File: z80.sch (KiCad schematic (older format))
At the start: 0 parts

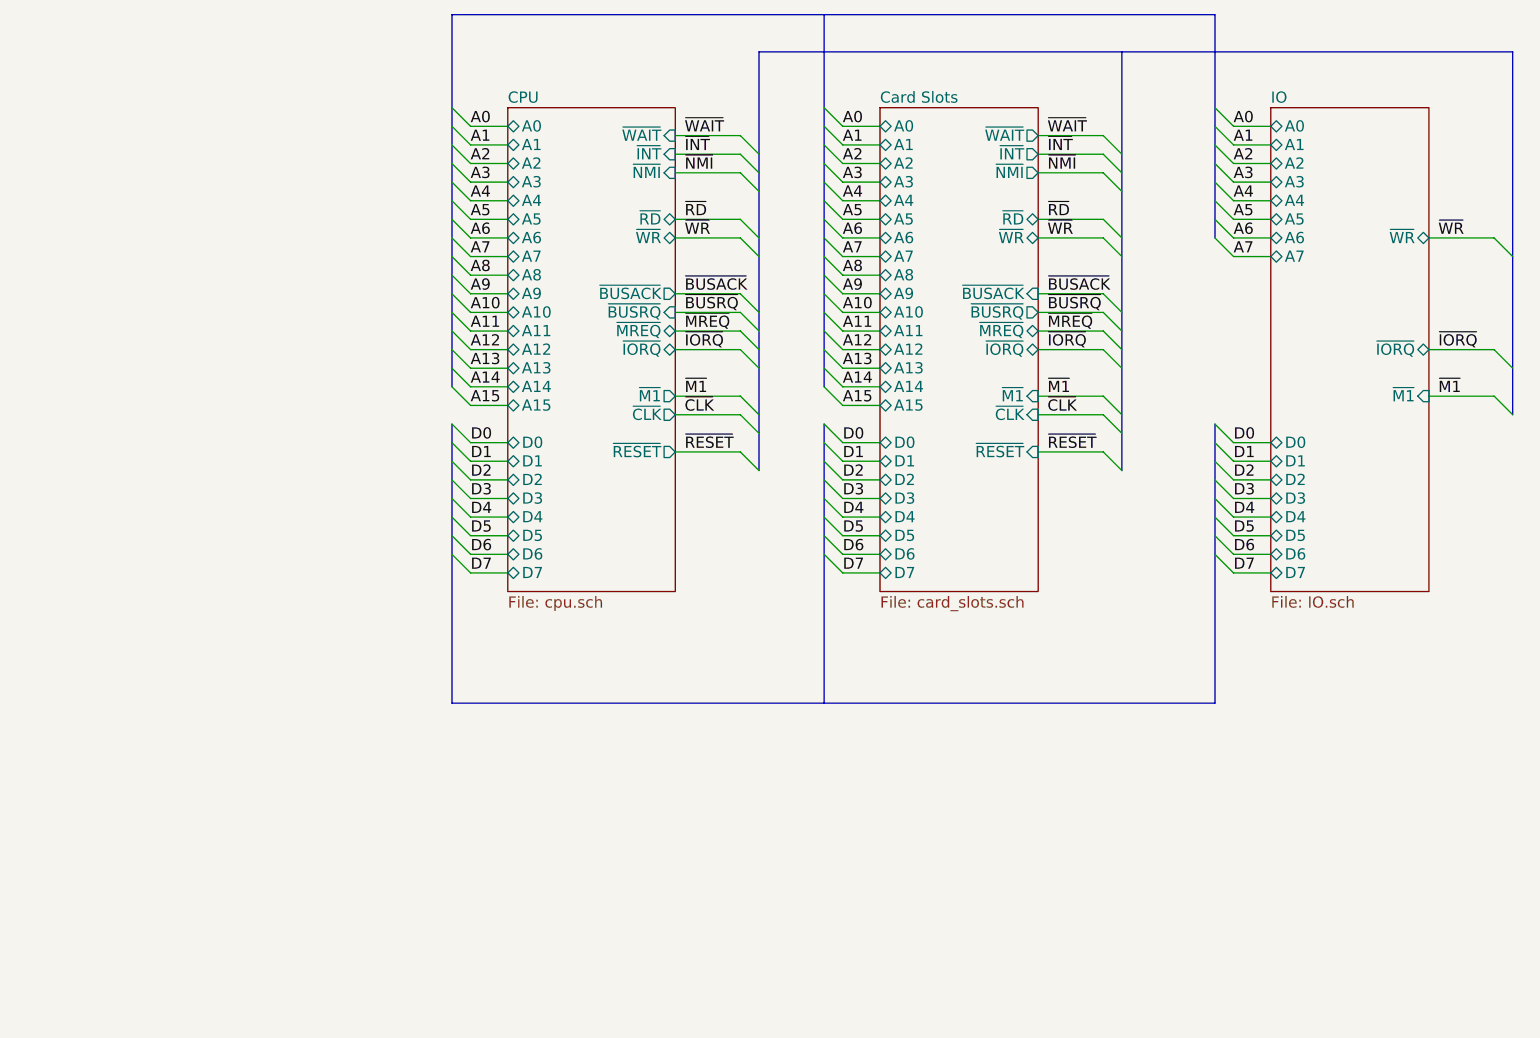
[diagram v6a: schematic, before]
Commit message: Added missing signals to IO and added buffer
I've removed the /WAIT and also added a somewhat dodgy diode AND to
handle the bi-directional Dx buffer. Might work, might not.

Also cleaned up the buses and just tidied things up.
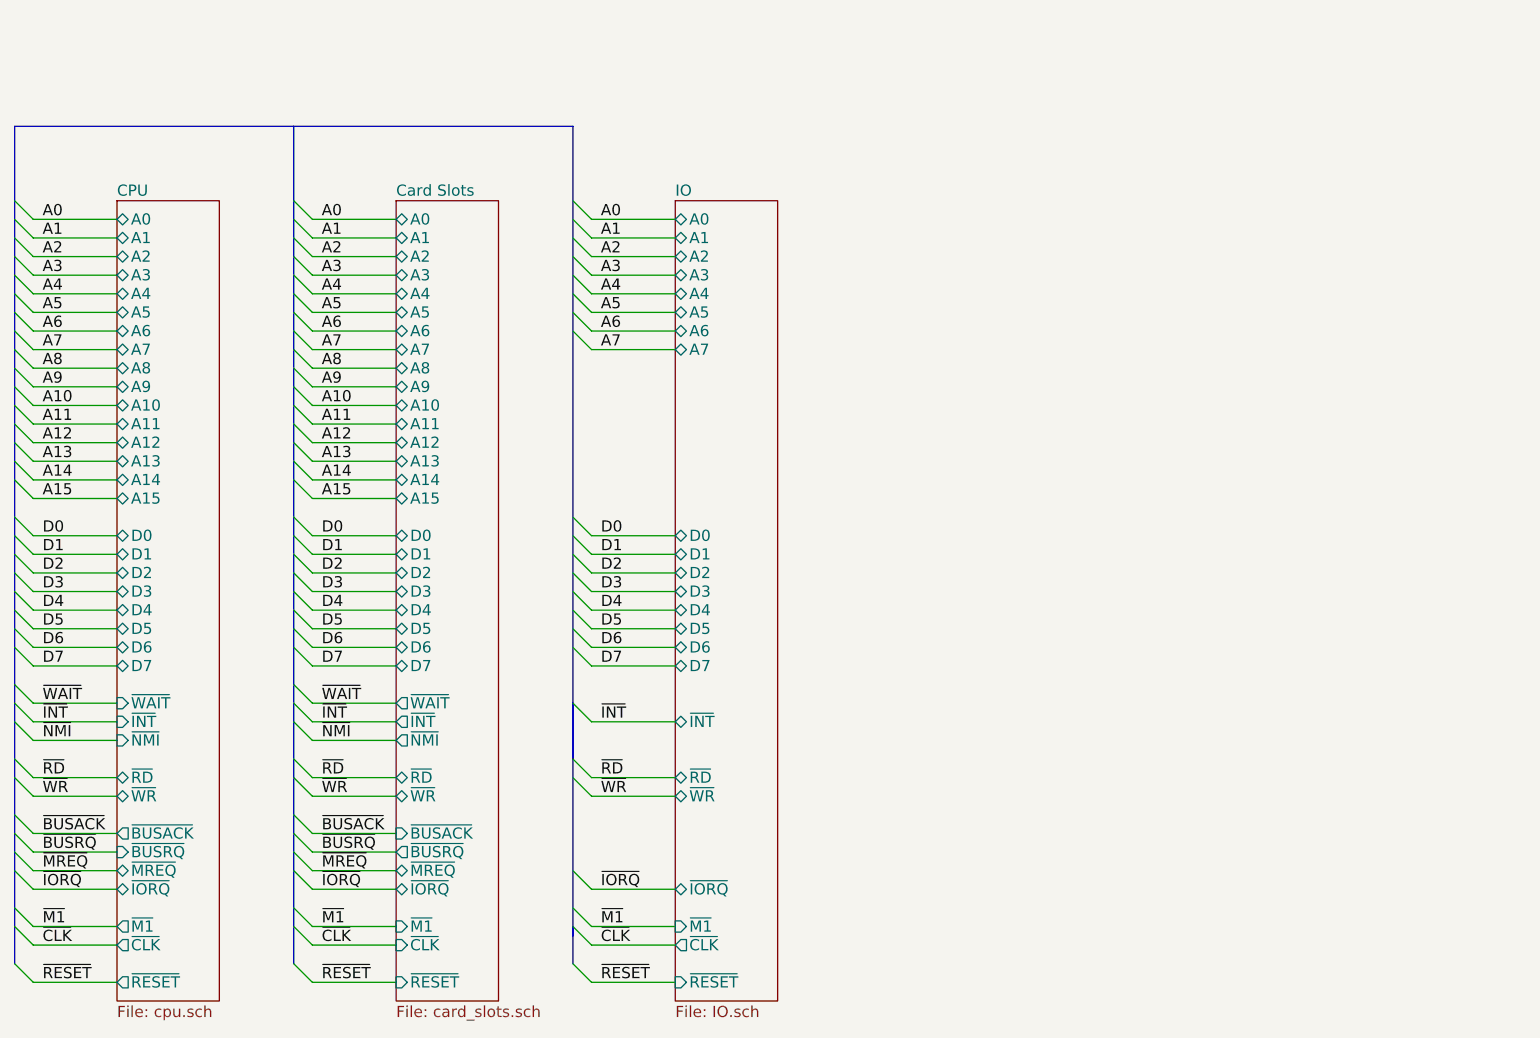
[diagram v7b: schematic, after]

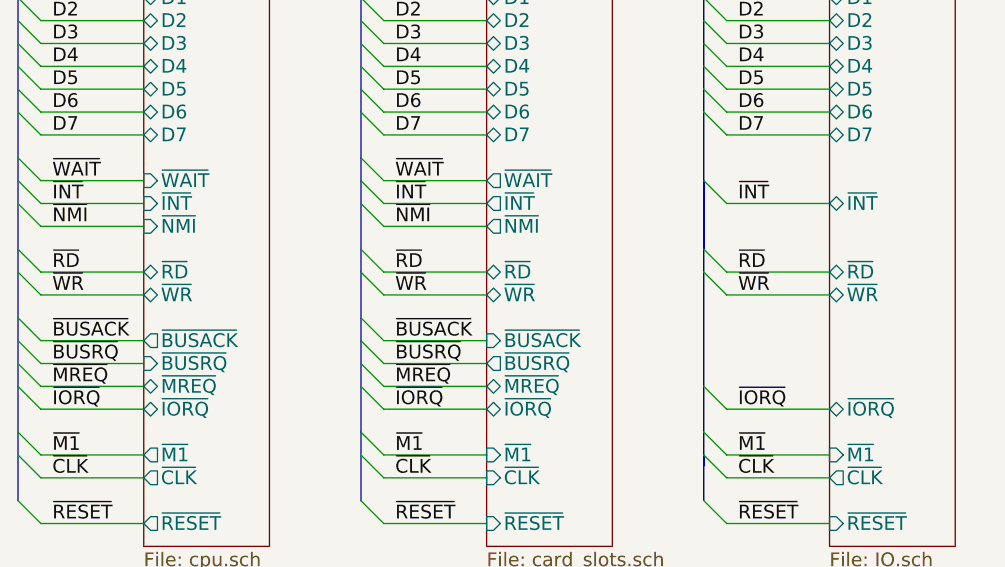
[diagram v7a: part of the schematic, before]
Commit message: Added /intack signal and a pri-encoder for /iosel
Brain fart on the diode crap. Was tired. Added a priority encoder to
enable the Dx buffer so it properly tristates when no IObus ports are
selected.

Added a NOR gate to provide a /intack signal for any board to properly
detect their interupt has been accepted but the z80. Boards will need to
figure out who the interupt is for.

Will have to add interupt priority pins to the boards to allow the
boards to put jump vectors onto the data bus to service the interrupt
This should be fairly easy, just means the service pritority of the
slots will be A-H, with A being the highest priority and H being the
lowest.

Going to replace the hex inverters with the spare NOR gates too.
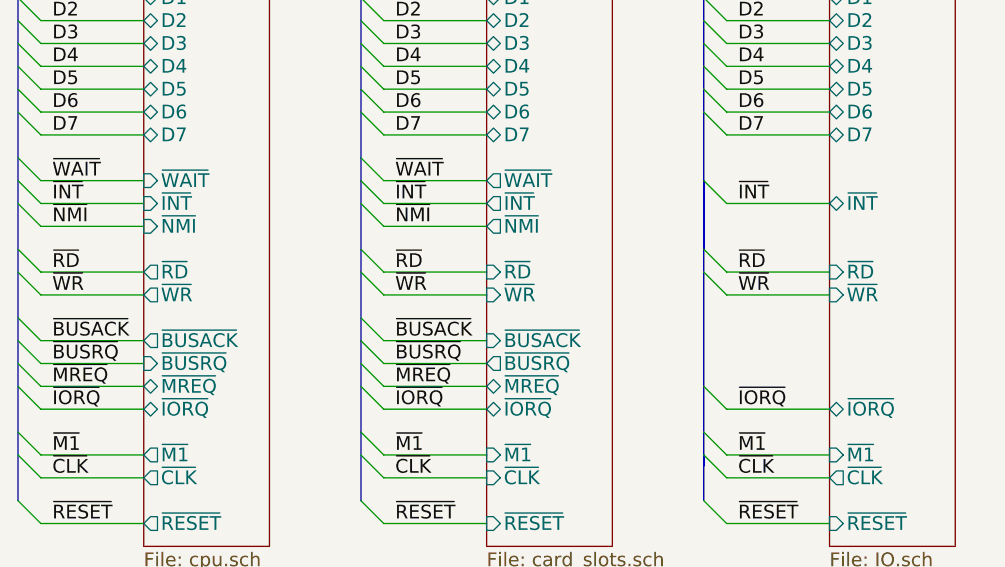
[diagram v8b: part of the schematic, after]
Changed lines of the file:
@@
 $Descr A4 11693 8268
 encoding utf-8
-Sheet 1 16
+Sheet 1 14
 Title ""
 Date ""
@@
 F25 "D7" T L 1500 4400 60
 F26 "~INT" I L 1500 4700 60
-F27 "~RD" T L 1500 5000 60
-F28 "~WR" T L 1500 5100 60
+F27 "~RD" O L 1500 5000 60
+F28 "~WR" O L 1500 5100 60
 F29 "~M1" O L 1500 5800 60
 F30 "~BUSACK" O L 1500 5300 60
@@
 F18 "~IORQ" T L 4500 5600 60
 F19 "~M1" I L 4500 5800 60
-F20 "~WR" T L 4500 5100 60
-F21 "~RD" T L 4500 5000 60
-F23 "~INT" B L 4500 4700 60
-F24 "~CLK" O L 4500 5900 60
-F25 "~RESET" I L 4500 6100 60
+F20 "~WR" I L 4500 5100 60
+F21 "~RD" I L 4500 5000 60
+F22 "~INT" B L 4500 4700 60
+F23 "~CLK" O L 4500 5900 60
+F24 "~RESET" I L 4500 6100 60
 $EndSheet
 Entry Wire Line
@@
 F26 "~WAIT" O L 3000 4600 60
 F27 "~INT" O L 3000 4700 60
-F28 "~RD" T L 3000 5000 60
-F29 "~WR" T L 3000 5100 60
+F28 "~RD" I L 3000 5000 60
+F29 "~WR" I L 3000 5100 60
 F30 "~M1" I L 3000 5800 60
 F31 "~BUSACK" I L 3000 5300 60
